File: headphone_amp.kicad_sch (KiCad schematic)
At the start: 0 parts

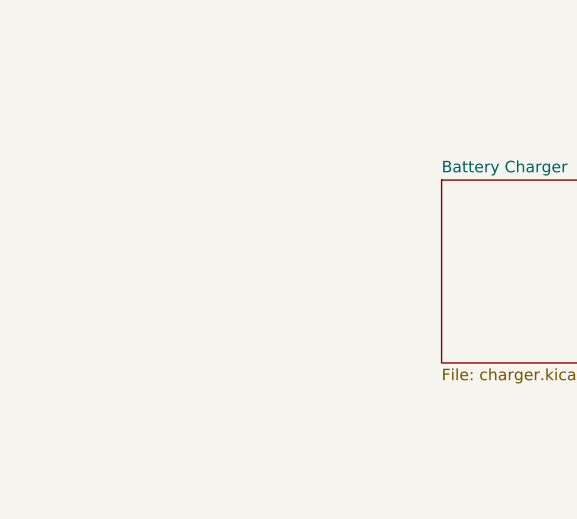
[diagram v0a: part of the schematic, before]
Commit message: Added USB power input and battery connector.
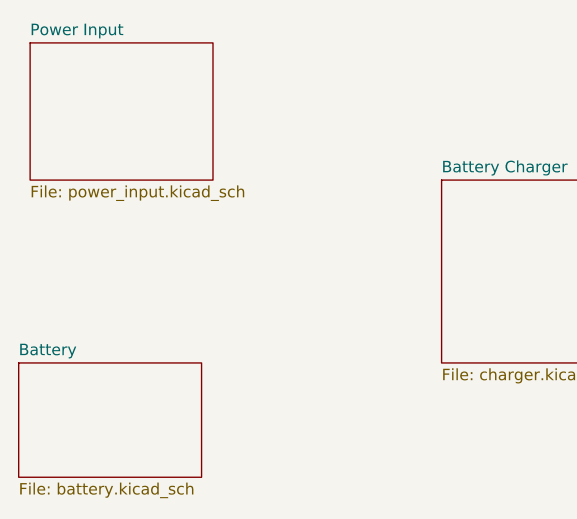
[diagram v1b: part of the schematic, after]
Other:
- added sheet Battery (battery.kicad_sch)
- added sheet Power Input (power_input.kicad_sch)
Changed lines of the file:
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@@
 	(paper "A4")
+	(sheet
+		(at 71.12 66.04)
+		(size 20.32 15.24)
+		(exclude_from_sim no)
+		(in_bom yes)
+		(on_board yes)
+		(dnp no)
+		(fields_autoplaced yes)
+		(stroke
+			(width 0.1524)
+			(type solid)
+		)
+		(fill
+			(color 0 0 0 0)
+		)
+		(property "Sheetname" "Power Input"
+			(at 71.12 65.3284 0)
+			(show_name no)
+			(do_not_autoplace no)
+			(effects
+				(font
+					(size 1.27 1.27)
+				)
+				(justify left bottom)
+			)
+		)
+		(property "Sheetfile" "power_input.kicad_sch"
+			(at 71.12 81.8646 0)
+			(show_name no)
+			(do_not_autoplace no)
+			(effects
+				(font
+					(size 1.27 1.27)
+				)
+				(justify left top)
+			)
+		)
+		(instances
+			(project "headphone_amp"
+				(path "/62ffec33-ae93-49a8-bfe6-566578dd8e82"
+					(page "3")
+				)
+			)
+		)
+	)
+	(sheet
+		(at 69.85 101.6)
+		(size 20.32 12.7)
+		(exclude_from_sim no)
+		(in_bom yes)
+		(on_board yes)
+		(dnp no)
+		(fields_autoplaced yes)
+		(stroke
+			(width 0.1524)
+			(type solid)
+		)
+		(fill
+			(color 0 0 0 0)
+		)
+		(property "Sheetname" "Battery"
+			(at 69.85 100.8884 0)
+			(show_name no)
+			(do_not_autoplace no)
+			(effects
+				(font
+					(size 1.27 1.27)
+				)
+				(justify left bottom)
+			)
+		)
+		(property "Sheetfile" "battery.kicad_sch"
+			(at 69.85 114.8846 0)
+			(show_name no)
+			(do_not_autoplace no)
+			(effects
+				(font
+					(size 1.27 1.27)
+				)
+				(justify left top)
+			)
+		)
+		(instances
+			(project "headphone_amp"
+				(path "/62ffec33-ae93-49a8-bfe6-566578dd8e82"
+					(page "4")
+				)
+			)
+		)
+	)
 	(sheet
 		(at 116.84 81.28)

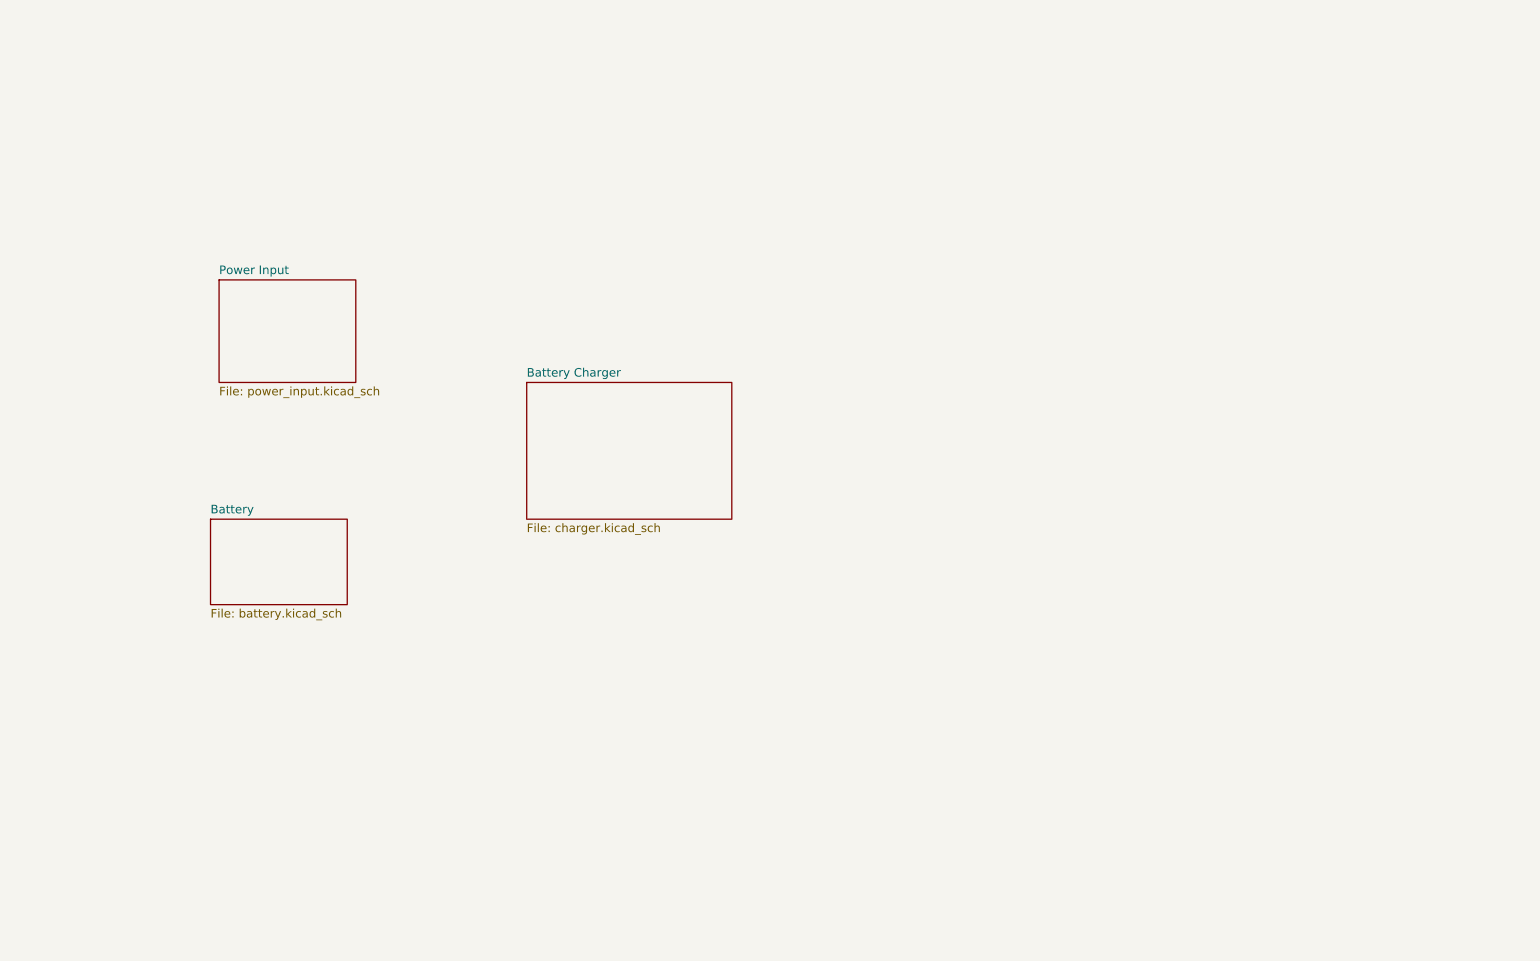
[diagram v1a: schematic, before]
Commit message: Started working on the audio input, including a rough-draft of the first stage.
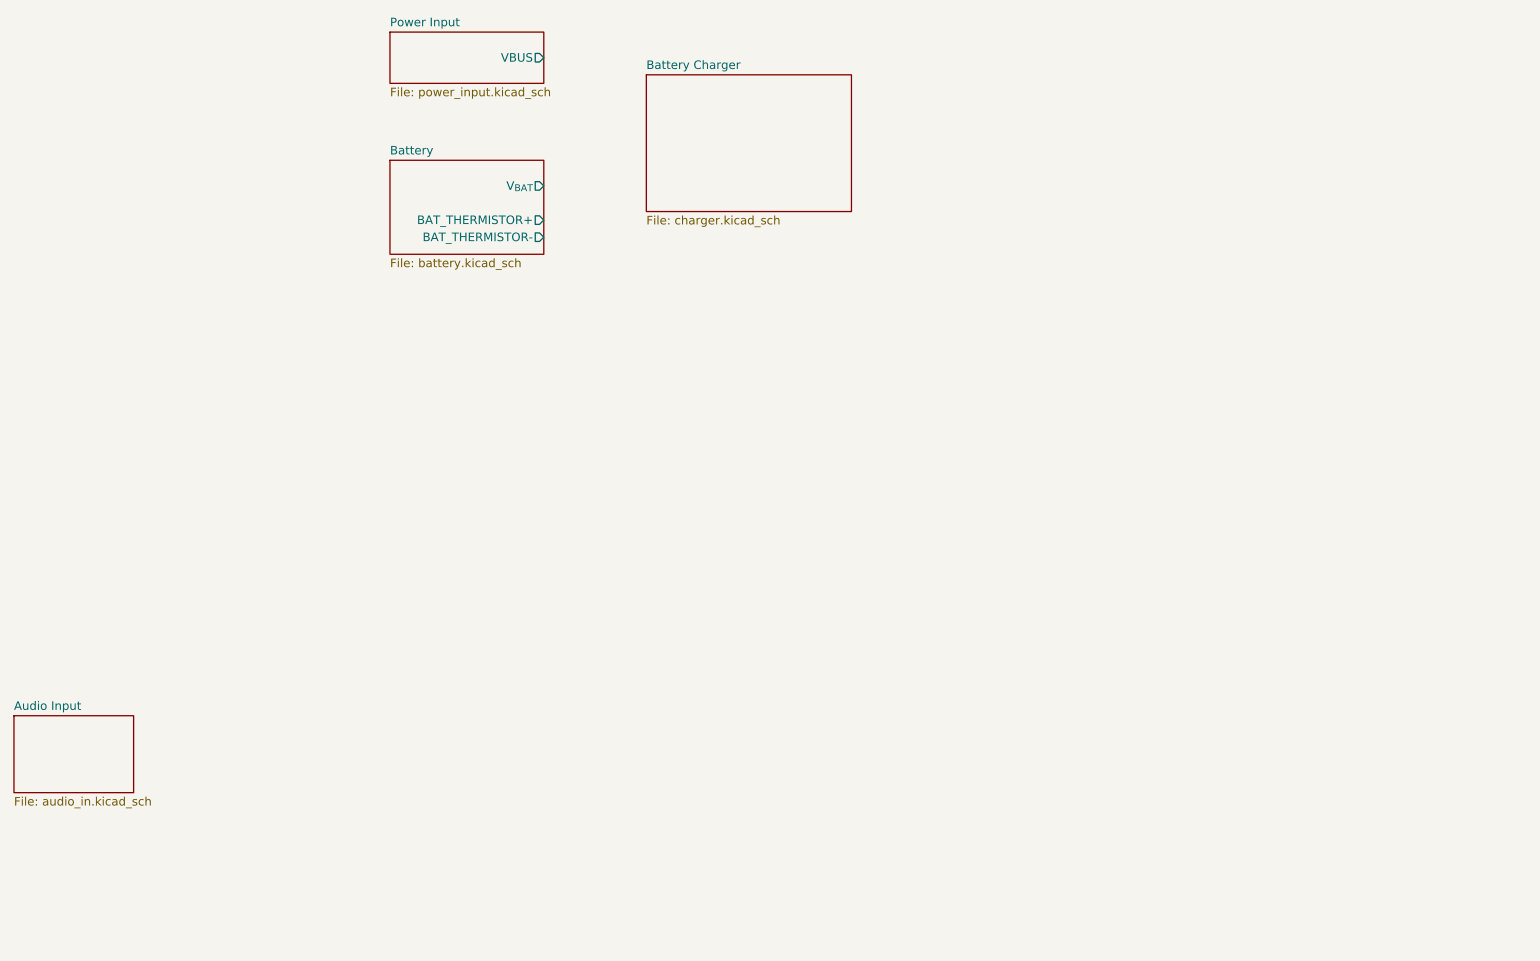
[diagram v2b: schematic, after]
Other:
- added sheet Audio Input (audio_in.kicad_sch)
- sheet Battery ports: added BAT_THERMISTOR+, BAT_THERMISTOR-, V_{BAT}; removed none
- sheet Power Input ports: added VBUS; removed none
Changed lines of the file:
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@@
 	(paper "A4")
 	(sheet
-		(at 71.12 66.04)
-		(size 20.32 15.24)
+		(at 96.52 29.21)
+		(size 22.86 7.62)
 		(exclude_from_sim no)
 		(in_bom yes)
@@
 		)
 		(property "Sheetname" "Power Input"
-			(at 71.12 65.3284 0)
+			(at 96.52 28.4984 0)
 			(show_name no)
 			(do_not_autoplace no)
@@
 		)
 		(property "Sheetfile" "power_input.kicad_sch"
-			(at 71.12 81.8646 0)
-			(show_name no)
-			(do_not_autoplace no)
-			(effects
-				(font
-					(size 1.27 1.27)
-				)
-				(justify left top)
+			(at 96.52 37.4146 0)
+			(show_name no)
+			(do_not_autoplace no)
+			(effects
+				(font
+					(size 1.27 1.27)
+				)
+				(justify left top)
+			)
+		)
+		(pin "VBUS" output
+			(at 119.38 33.02 0)
+			(effects
+				(font
+					(size 1.27 1.27)
+				)
+				(justify right)
 			)
 		)
@@
 	)
 	(sheet
-		(at 69.85 101.6)
-		(size 20.32 12.7)
+		(at 96.52 48.26)
+		(size 22.86 13.97)
 		(exclude_from_sim no)
 		(in_bom yes)
@@
 		)
 		(property "Sheetname" "Battery"
-			(at 69.85 100.8884 0)
+			(at 96.52 47.5484 0)
 			(show_name no)
 			(do_not_autoplace no)
@@
 		)
 		(property "Sheetfile" "battery.kicad_sch"
-			(at 69.85 114.8846 0)
-			(show_name no)
-			(do_not_autoplace no)
-			(effects
-				(font
-					(size 1.27 1.27)
-				)
-				(justify left top)
+			(at 96.52 62.8146 0)
+			(show_name no)
+			(do_not_autoplace no)
+			(effects
+				(font
+					(size 1.27 1.27)
+				)
+				(justify left top)
+			)
+		)
+		(pin "BAT_THERMISTOR+" output
+			(at 119.38 57.15 0)
+			(effects
+				(font
+					(size 1.27 1.27)
+				)
+				(justify right)
+			)
+		)
+		(pin "BAT_THERMISTOR-" output
+			(at 119.38 59.69 0)
+			(effects
+				(font
+					(size 1.27 1.27)
+				)
+				(justify right)
+			)
+		)
+		(pin "V_{BAT}" output
+			(at 119.38 52.07 0)
+			(effects
+				(font
+					(size 1.27 1.27)
+				)
+				(justify right)
 			)
 		)
@@
 	)
 	(sheet
-		(at 116.84 81.28)
+		(at 134.62 35.56)
 		(size 30.48 20.32)
 		(exclude_from_sim no)
@@
 		)
 		(property "Sheetname" "Battery Charger"
-			(at 116.84 80.5684 0)
+			(at 134.62 34.8484 0)
 			(show_name no)
 			(do_not_autoplace no)
@@
 		)
 		(property "Sheetfile" "charger.kicad_sch"
-			(at 116.84 102.1846 0)
+			(at 134.62 56.4646 0)
 			(show_name no)
 			(do_not_autoplace no)
@@
 				)
 			)
+		)
+	)
+	(sheet
+		(at 40.64 130.81)
+		(size 17.78 11.43)
+		(exclude_from_sim no)
+		(in_bom yes)
+		(on_board yes)
+		(dnp no)
+		(fields_autoplaced yes)
+		(stroke
+			(width 0.1524)
+			(type solid)
+		)
+		(fill
+			(color 0 0 0 0)
+		)
+		(property "Sheetname" "Audio Input"
+			(at 40.64 130.0984 0)
+			(show_name no)
+			(do_not_autoplace no)
+			(effects
+				(font
+					(size 1.27 1.27)
+				)
+				(justify left bottom)
+			)
+		)
+		(property "Sheetfile" "audio_in.kicad_sch"
+			(at 40.64 142.8246 0)
+			(show_name no)
+			(do_not_autoplace no)
+			(effects
+				(font
+					(size 1.27 1.27)
+				)
+				(justify left top)
+			)
+		)
+		(instances
+			(project "headphone_amp"
+				(path "/62ffec33-ae93-49a8-bfe6-566578dd8e82"
+					(page "5")
+				)
+			)

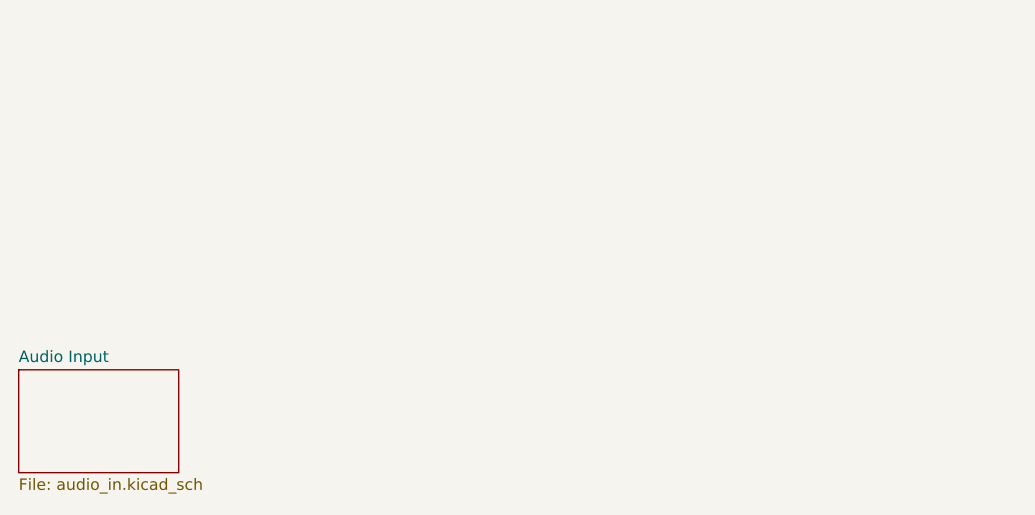
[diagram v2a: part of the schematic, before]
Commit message: Finished second stage, added diode clipping options, and started current buffer.
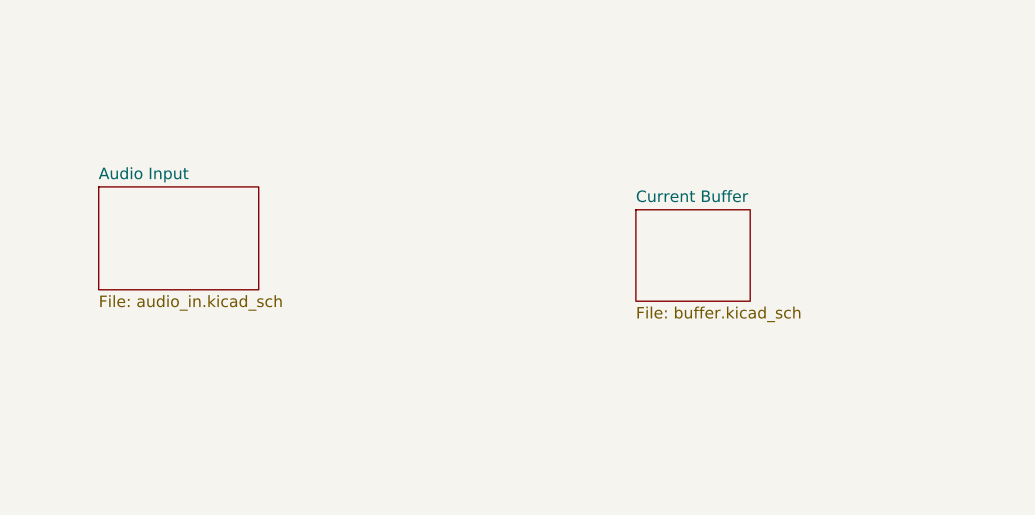
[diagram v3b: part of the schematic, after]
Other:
- added sheet Current Buffer (buffer.kicad_sch)
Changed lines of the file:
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@@
 	)
 	(sheet
-		(at 40.64 130.81)
+		(at 109.22 113.03)
+		(size 12.7 10.16)
+		(exclude_from_sim no)
+		(in_bom yes)
+		(on_board yes)
+		(dnp no)
+		(fields_autoplaced yes)
+		(stroke
+			(width 0.1524)
+			(type solid)
+		)
+		(fill
+			(color 0 0 0 0)
+		)
+		(property "Sheetname" "Current Buffer"
+			(at 109.22 112.3184 0)
+			(show_name no)
+			(do_not_autoplace no)
+			(effects
+				(font
+					(size 1.27 1.27)
+				)
+				(justify left bottom)
+			)
+		)
+		(property "Sheetfile" "buffer.kicad_sch"
+			(at 109.22 123.7746 0)
+			(show_name no)
+			(do_not_autoplace no)
+			(effects
+				(font
+					(size 1.27 1.27)
+				)
+				(justify left top)
+			)
+		)
+		(instances
+			(project "headphone_amp"
+				(path "/62ffec33-ae93-49a8-bfe6-566578dd8e82"
+					(page "6")
+				)
+			)
+		)
+	)
+	(sheet
+		(at 49.53 110.49)
 		(size 17.78 11.43)
 		(exclude_from_sim no)
@@
 		)
 		(property "Sheetname" "Audio Input"
-			(at 40.64 130.0984 0)
+			(at 49.53 109.7784 0)
 			(show_name no)
 			(do_not_autoplace no)
@@
 		)
 		(property "Sheetfile" "audio_in.kicad_sch"
-			(at 40.64 142.8246 0)
+			(at 49.53 122.5046 0)
 			(show_name no)
 			(do_not_autoplace no)
